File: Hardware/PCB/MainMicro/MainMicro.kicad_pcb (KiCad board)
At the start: 2 copper layers, 64.8 x 54.6 mm, 61 parts, among them J1 Conn_02x05_Odd_Even, J10 Conn_01x03_Male, J11 Conn_01x05_Male, J12 Conn_01x05_Male, J2 USB_B_Mini, J3 Barrel_Jack, J4 Conn_01x05_Male, J5 Conn_01x06_Male, J6 Conn_01x06_Male, J7 Conn_01x03_Male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

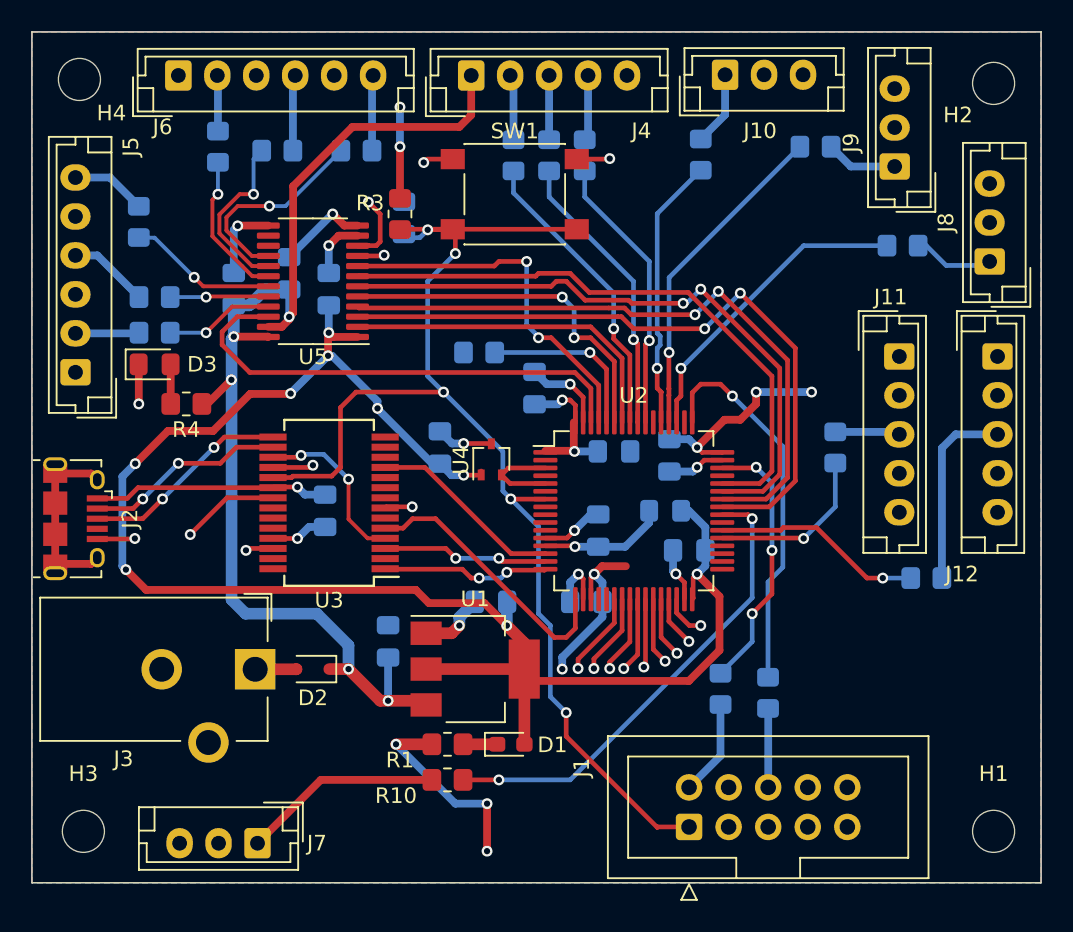
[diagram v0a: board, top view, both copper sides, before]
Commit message: Added Logic translation for SPI
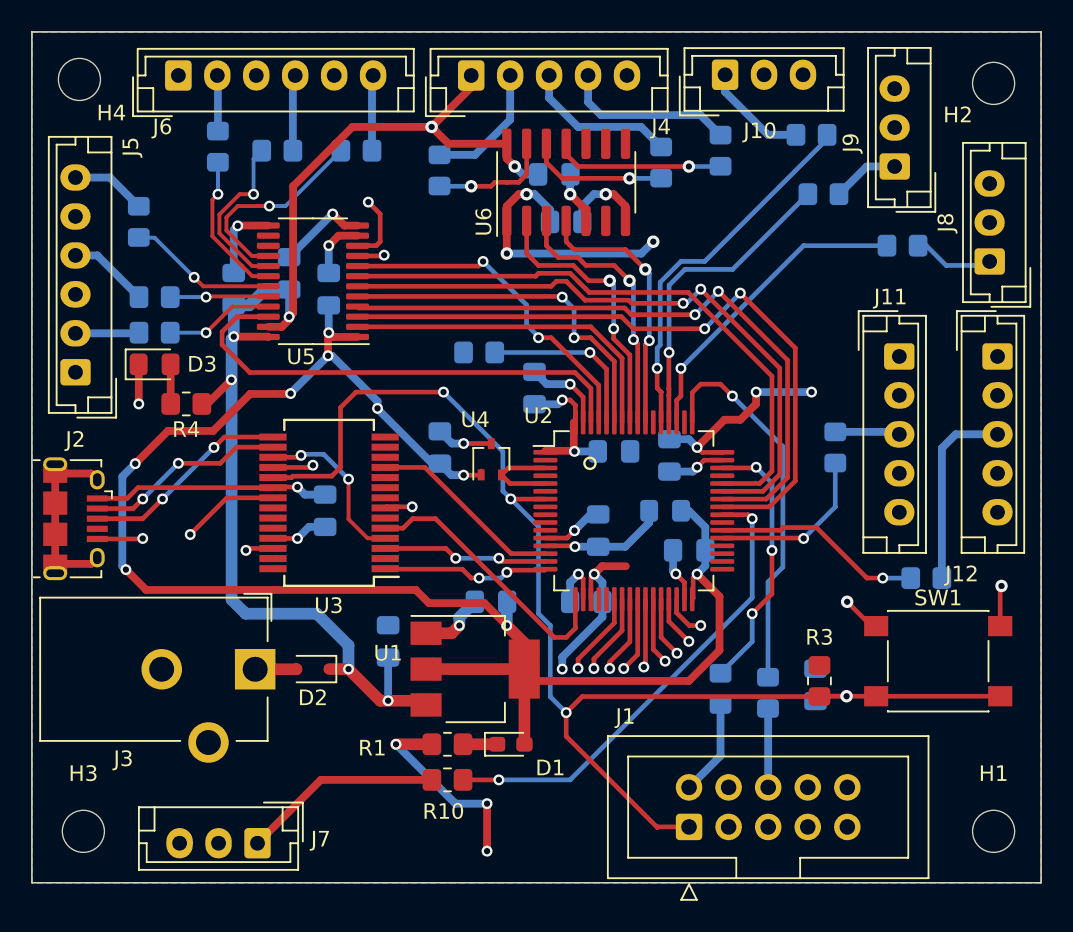
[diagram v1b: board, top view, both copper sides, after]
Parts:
- added C12: .1u, Capacitor_SMD:C_0805_2012Metric_Pad1.18x1.45mm_HandSolder, B.Cu at (180.8, 75.2)
- added C16: .1u, Capacitor_SMD:C_0805_2012Metric_Pad1.18x1.45mm_HandSolder, B.Cu at (181.6, 78.2)
- added U6: TXB0104D, Package_SO:SOIC-14_3.9x8.7mm_P1.27mm, F.Cu at (181.6, 75.7)
- moved SW1 40.5 mm to (205.5, 106.4)
- moved R3 40.3 mm to (197.9, 107.7)
- moved C3 40.0 mm to (197.6, 108.0)
- moved R5 8.72 mm to (191.5, 73.7)
- moved R13 7.22 mm to (197.4, 72.6), turned to 180 degrees
- moved R7 7.21 mm to (187.7, 74.4)
- moved R6 4.84 mm to (173.5, 74.9)
- moved R12 3.09 mm to (198.1, 76.5)
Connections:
- net Net-(D2-Pad2) renamed /BJ5V
- R5 pad 2: /SPI1_SCK -> /SPI1_SCK_5V
- R6 pad 2: /SPI1_MOSI -> /SPI1_MOSI_5V
- R7 pad 2: /SPI1_MISO -> /SPI1_MISO_5V
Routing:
- net +3V3: track 148.4 -> 159.6 mm, vias 18 -> 19
- net /SPI1_SCK_5V: track 0.00 -> 10.9 mm, vias 0 -> 1
- net GND: track 87.4 -> 97.7 mm, vias 24 -> 26
- net /SPI1_MISO_5V: track 0.00 -> 9.00 mm, vias 0 -> 1
- net /SPI1_MOSI_5V: track 0.00 -> 7.88 mm, vias 0 -> 1
- net +5V: track 75.7 -> 83.3 mm, vias 5 -> 7
- net Net-(J4-Pad4): track 4.21 -> 11.1 mm
- net /Limit_SW4: track 17.6 -> 24.0 mm
- net Net-(J4-Pad3): track 4.13 -> 9.94 mm
- net Net-(J4-Pad2): track 4.21 -> 8.30 mm
- net /NRST: track 79.9 -> 83.8 mm, vias 5 -> 4
- net Net-(J10-Pad1): track 4.77 -> 6.79 mm
- net /PB8_GPO: track 23.7 -> 22.1 mm
- net /SPI1_MOSI: track 19.2 -> 17.8 mm, vias 1 -> 2
- net /SPI1_MISO: track 18.5 -> 17.2 mm, vias 1 -> 2
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
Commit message: Please don't break
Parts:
- added C17: 100n, Capacitor_SMD:C_0805_2012Metric_Pad1.18x1.45mm_HandSolder, F.Cu at (166.4, 113.0)
- added J13: Conn_01x04_Female, Connector_JST:JST_EH_B4B-EH-A_1x04_P2.50mm_Vertical, F.Cu at (168.1, 91.7)
- added J14: Conn_01x02_Male, Connector_JST:JST_EH_B2B-EH-A_1x02_P2.50mm_Vertical, F.Cu at (169.7, 117.9)
- added R22: 100k, Resistor_SMD:R_0805_2012Metric_Pad1.20x1.40mm_HandSolder, F.Cu at (168.9, 111.0)
- added R23: 10, Resistor_SMD:R_0805_2012Metric_Pad1.20x1.40mm_HandSolder, F.Cu at (173.0, 113.0)
- U3: value FT232RL -> FT231XS; footprint Package_SO:SSOP-28_5.3x10.2mm_P0.65mm -> Package_SO:SSOP-20_3.9x8.7mm_P0.635mm
- moved D1 26.6 mm to (152.1, 105.7), turned to 90 degrees
- moved R1 25.1 mm to (149.6, 105.7), turned to 90 degrees
- moved J7 19.1 mm to (180.8, 117.9)
- moved C10 7.46 mm to (158.8, 97.8), turned to -90 degrees
- moved R10 5.84 mm to (179.8, 114.0)
- moved U3 5.20 mm to (161.3, 97.3)
- moved J3 2.77 mm to (159.0, 106.1), turned to 0 degrees
- moved D2 2.27 mm to (166.4, 104.9)
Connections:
- net /SPI1_MISO renamed /SPI1_LATCH
- net /SPI1_MISO_5V renamed /SPI1_LATCH_5V
- U2 pad 22: /PA6 -> /PA6_GPI
- U3 pad 1: /USART2_TX -> unconnected-(U3-Pad1)
- U3 pad 11: /USART2_CTS -> /USB_D+
- U3 pad 12: unconnected-(U3-Pad12) -> /USB_D-
- U3 pad 13: unconnected-(U3-Pad13) -> Net-(U3-Pad13)
- U3 pad 14: unconnected-(U3-Pad14) -> /NRST
- U3 pad 15: /USB_D+ -> Net-(U3-Pad13)
- U3 pad 16: /USB_D- -> GND
- U3 pad 17: Net-(U3-Pad17) -> unconnected-(U3-Pad17)
- U3 pad 18: GND -> unconnected-(U3-Pad18)
- U3 pad 19: /NRST -> unconnected-(U3-Pad19)
- U3 pad 2: unconnected-(U3-Pad2) -> /USART2_RTS
- U3 pad 20: /VUSB 5V -> /USART2_TX
- U3 pad 3: /USART2_RTS -> /VUSB 5V
- U3 pad 4: Net-(U3-Pad17) -> /USART2_RX
- U3 pad 5: /USART2_RX -> unconnected-(U3-Pad5)
- U3 pad 6: unconnected-(U3-Pad6) -> GND
- U3 pad 7: GND -> unconnected-(U3-Pad7)
- U3 pad 8: (no net) -> unconnected-(U3-Pad8)
- U3 pad 9: unconnected-(U3-Pad9) -> /USART2_CTS
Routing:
- net /PA6_GPI: track 0.00 -> 18.1 mm, vias 0 -> 2
- net /USART2_TX: track 10.8 -> 24.0 mm
- net /USART2_RTS: track 10.6 -> 22.4 mm, vias 2 -> 3
- net Net-(C17-Pad1): track 0.00 -> 11.7 mm, vias 0 -> 1
- net Net-(U3-Pad17): track 11.0 -> 0.00 mm, vias 2 -> 0
- net +3V3: track 159.6 -> 170.0 mm, vias 19 -> 20
- net /USART2_CTS: track 12.6 -> 21.8 mm
- net Net-(J7-Pad1): track 12.9 -> 4.69 mm
- net /USART2_RX: track 17.7 -> 24.5 mm, vias 0 -> 1
- net /Limit_SW1: track 30.5 -> 24.8 mm
- net /NRST: track 83.8 -> 89.3 mm
- net /PA6: track 5.41 -> 0.00 mm, vias 1 -> 0
- net Net-(U3-Pad13): track 0.00 -> 4.26 mm
- net /BJ5V: track 2.66 -> 6.79 mm
- net GND: track 97.7 -> 94.4 mm, vias 26 -> 23
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
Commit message: Commit for PCB final
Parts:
- moved H2 0.25 mm to (208.8, 69.3)
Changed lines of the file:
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@@
   )
   (footprint "MountingHole:MountingHole_2.7mm_M2.5" (layer "F.Cu")
-    (at 209.042 69.342)
+    (at 208.788 69.342)
     (descr "Mounting Hole 2.7mm, no annular, M2.5")
     (tags "mounting hole 2.7mm no annular m2.5")

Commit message: Generated Main Micro Gerber Files
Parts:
- moved U4 1.86 mm to (176.3, 91.7)
- moved C11 1.15 mm to (173.0, 91.7)
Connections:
- U2 pad 3: /8MHz_OSC_IN -> unconnected-(U2-Pad3)
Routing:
- net +3V3: track 170.0 -> 168.7 mm
- net /8MHz_OSC_IN: track 6.05 -> 5.04 mm

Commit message: Post joe
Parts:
- removed D2: BAT60JFILM, Diode_SMD:D_SOD-323
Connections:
- J3 pad 1: /BJ5V -> +5V
- U2 pad 58: /PB6_GPO -> unconnected-(U2-Pad58)
- U5 pad 2: /PB6_GPO -> +3V3
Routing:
- net /PB6_GPO: track 21.9 -> 0.00 mm
- net +5V: track 80.5 -> 88.8 mm
- net /BJ5V: track 6.79 -> 0.00 mm
- net +3V3: track 168.7 -> 170.9 mm
